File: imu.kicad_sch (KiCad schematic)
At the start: 2 parts, among them U1 BMI088

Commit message: Updated stm32
Updated stm32 and usb-c
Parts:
- renumbered C3 to C8
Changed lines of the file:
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@@
 	(wire
 		(pts
-			(xy 130.81 92.71) (xy 133.35 92.71)
+			(xy 129.54 92.71) (xy 133.35 92.71)
 		)
 		(stroke
@@
 		)
 	)
-	(hierarchical_label "IMU_SDA"
-		(shape passive)
-		(at 130.81 92.71 180)
-		(effects
-			(font
-				(size 1.27 1.27)
-			)
-			(justify right)
-		)
-	)
-	(hierarchical_label "IMU_SCL"
+	(global_label "INT_ACC"
+		(shape output)
+		(at 163.83 85.09 0)
+		(fields_autoplaced yes)
+		(effects
+			(font
+				(size 1.27 1.27)
+			)
+			(justify left)
+		)
+		(property "Intersheetrefs" "${INTERSHEET_REFS}"
+			(at 174.3143 85.09 0)
+			(hide yes)
+			(show_name no)
+			(do_not_autoplace no)
+			(effects
+				(font
+					(size 1.27 1.27)
+				)
+				(justify left)
+			)
+		)
+	)
+	(global_label "INT_GYR"
+		(shape output)
+		(at 163.83 90.17 0)
+		(fields_autoplaced yes)
+		(effects
+			(font
+				(size 1.27 1.27)
+			)
+			(justify left)
+		)
+		(property "Intersheetrefs" "${INTERSHEET_REFS}"
+			(at 174.3143 90.17 0)
+			(hide yes)
+			(show_name no)
+			(do_not_autoplace no)
+			(effects
+				(font
+					(size 1.27 1.27)
+				)
+				(justify left)
+			)
+		)
+	)
+	(global_label "IMU_SCL"
 		(shape input)
 		(at 130.81 90.17 180)
+		(fields_autoplaced yes)
 		(effects
 			(font
@@
 			(justify right)
 		)
-	)
-	(hierarchical_label "INT_GYR"
-		(shape output)
-		(at 163.83 90.17 0)
-		(effects
-			(font
-				(size 1.27 1.27)
-			)
-			(justify left)
-		)
-	)
-	(hierarchical_label "INT_ACC"
-		(shape output)
-		(at 163.83 85.09 0)
-		(effects
-			(font
-				(size 1.27 1.27)
-			)
-			(justify left)
+		(property "Intersheetrefs" "${INTERSHEET_REFS}"
+			(at 119.9629 90.17 0)
+			(hide yes)
+			(show_name no)
+			(do_not_autoplace no)
+			(effects
+				(font
+					(size 1.27 1.27)
+				)
+				(justify right)
+			)
+		)
+	)
+	(global_label "IMU_SDA"
+		(shape passive)
+		(at 129.54 92.71 180)
+		(fields_autoplaced yes)
+		(effects
+			(font
+				(size 1.27 1.27)
+			)
+			(justify right)
+		)
+		(property "Intersheetrefs" "${INTERSHEET_REFS}"
+			(at 119.7437 92.71 0)
+			(hide yes)
+			(show_name no)
+			(do_not_autoplace no)
+			(effects
+				(font
+					(size 1.27 1.27)
+				)
+				(justify right)
+			)
 		)
 	)
@@
 		(in_pos_files yes)
 		(dnp no)
-		(property "Reference" "C3"
+		(property "Reference" "C8"
 			(at 110.49 92.7099 0)
 			(show_name no)
@@
 			(project "Drone_FC_project"
 				(path "/3077c137-9a1a-496f-be15-3587b3336d21/ee62e42c-1ca0-4e46-9141-f640bba8485d"
-					(reference "C3")
+					(reference "C8")
 					(unit 1)
 				)

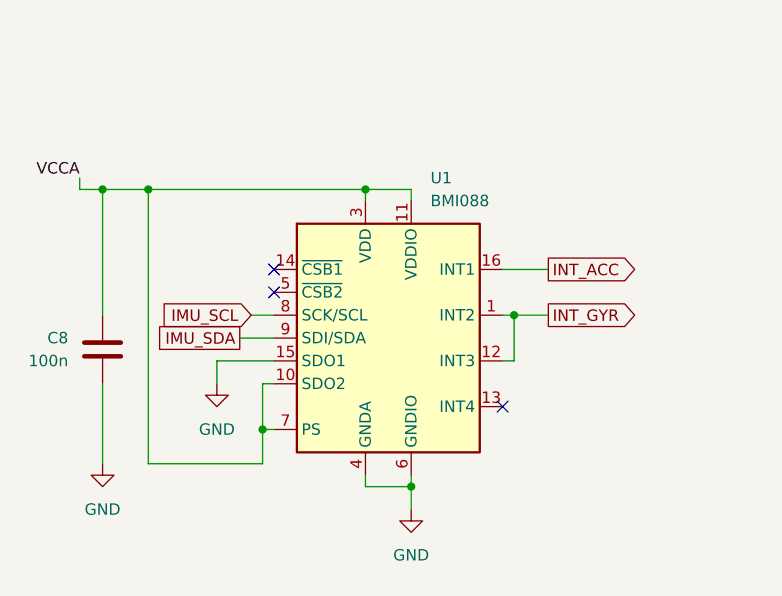
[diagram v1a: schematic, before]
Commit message: IMU, VBAT_Sense,
Fixed some decoupling issues, made the IMU into SPI mode. Wired all to stm32. Few updates on the appearances as well to make it look more organized.
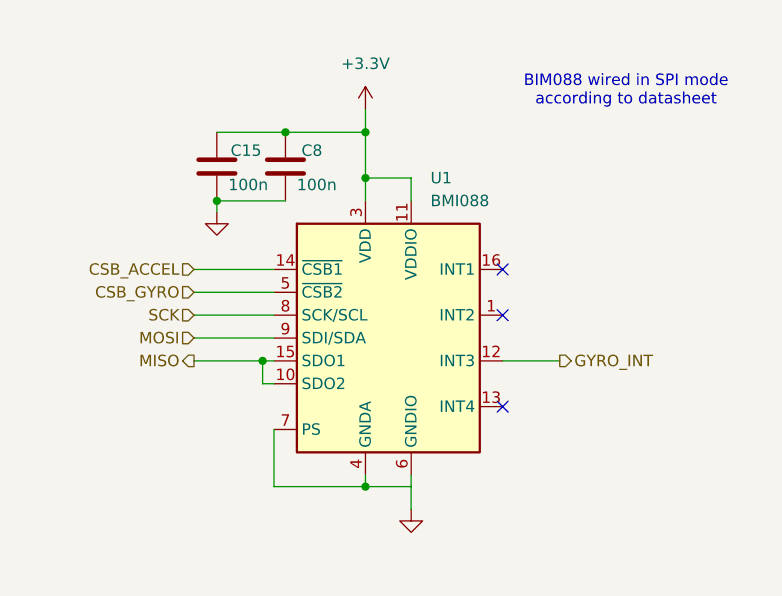
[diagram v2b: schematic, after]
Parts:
- added C15: 100n, Capacitor_SMD:C_0603_1608Metric, symbol Device:C
- C8: footprint Package_LGA:Bosch_LGA-16_4.5x3mm_P0.5mm_LayoutBorder7x1y_ClockwisePinNumbering -> Capacitor_SMD:C_0603_1608Metric
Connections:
- net GND: now also C15.2; no longer U1.15 (SDO1), U1.2 (GNDA), U1.4 (GNDA)
- net CSB_ACCEL: now reaches U1.14 (~{CSB1})
- net CSB_GYRO: now reaches U1.5 (~{CSB2})
- net IMU_SCL renamed SCK
- net IMU_SDA renamed MOSI
- net INT_ACC: no longer names the net of U1.16 (INT1)
- net INT_GYR: no longer names the net of U1.1 (INT2)
- net INT_GYR: no longer U1.12 (INT3)
- net VCCA renamed +3.3V
- net +3.3V: now also C15.1; no longer U1.10 (SDO2), U1.7 (PS)
- new net: U1.2 (GNDA), U1.4 (GNDA), U1.7 (PS)
- new net GYRO_INT: U1.12 (INT3)
- new net MISO: U1.10 (SDO2), U1.15 (SDO1)
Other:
- note added: "BIM088 wired in SPI mode according to datasheet"

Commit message: Created radio, cleanup a few other things
Finished radio schematic, added datasheets, added a stm32cubemx file for pinouts, added SPI1 and SPI2.
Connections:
- net MISO renamed SPI2_MISO
- net MOSI renamed SPI2_MOSI
- net SCK renamed SPI2_SCK
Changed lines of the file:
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@@
 		)
 	)
-	(hierarchical_label "MISO"
+	(hierarchical_label "SPI2_MISO"
 		(shape output)
 		(at 124.46 95.25 180)
@@
 		)
 	)
-	(hierarchical_label "SCK"
+	(hierarchical_label "SPI2_SCK"
 		(shape input)
 		(at 124.46 90.17 180)
@@
 		)
 	)
-	(hierarchical_label "MOSI"
+	(hierarchical_label "SPI2_MOSI"
 		(shape input)
 		(at 124.46 92.71 180)

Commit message: Fixing some radio things
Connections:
- net GND: now also U1.2 (GNDA), U1.4 (GNDA), U1.7 (PS)
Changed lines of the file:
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@@
 	(generator_version "10.0")
 	(paper "A4")
+	(rectangle
+		(start 109.22 57.15)
+		(end 181.61 119.38)
+		(stroke
+			(width 0)
+			(type default)
+		)
+		(fill
+			(type none)
+		)
+	)
 	(text "BIM088 wired in SPI mode\naccording to datasheet"
 		(exclude_from_sim no)
-		(at 172.466 65.278 0)
+		(at 165.1 66.04 0)
 		(effects
 			(font
@@
 	)
 	(junction
-		(at 143.51 109.22)
-		(diameter 0)
-		(color 0 0 0 0)
-	)
-	(junction
 		(at 143.51 74.93)
 		(diameter 0)
@@
 		(color 0 0 0 0)
 	)
+	(junction
+		(at 148.59 109.22)
+		(diameter 0)
+		(color 0 0 0 0)
+	)
 	(no_connect
 		(at 158.75 100.33)
@@
 	(wire
 		(pts
+			(xy 148.59 109.22) (xy 148.59 111.76)
+		)
+		(stroke
+			(width 0)
+			(type default)
+		)
+	)
+	(wire
+		(pts
 			(xy 124.46 85.09) (xy 133.35 85.09)
 		)
@@
 	(wire
 		(pts
+			(xy 132.08 102.87) (xy 133.35 102.87)
+		)
+		(stroke
+			(width 0)
+			(type default)
+		)
+	)
+	(wire
+		(pts
 			(xy 127 77.47) (xy 134.62 77.47)
 		)
@@
 	(wire
 		(pts
-			(xy 148.59 107.95) (xy 148.59 111.76)
+			(xy 148.59 107.95) (xy 148.59 109.22)
 		)
 		(stroke
@@
 	(wire
 		(pts
-			(xy 133.35 109.22) (xy 143.51 109.22)
-		)
-		(stroke
-			(width 0)
-			(type default)
-		)
-	)
-	(wire
-		(pts
-			(xy 143.51 109.22) (xy 148.59 109.22)
+			(xy 148.59 109.22) (xy 143.51 109.22)
 		)
 		(stroke
@@
 	(wire
 		(pts
-			(xy 133.35 102.87) (xy 133.35 109.22)
+			(xy 132.08 102.87) (xy 132.08 104.14)
 		)
 		(stroke
@@
 					(unit 1)
 				)
+			)
+		)
+	)
+	(symbol
+		(lib_id "power:GND")
+		(at 132.08 104.14 0)
+		(unit 1)
+		(body_style 1)
+		(exclude_from_sim no)
+		(in_bom yes)
+		(on_board yes)
+		(in_pos_files yes)
+		(dnp no)
+		(fields_autoplaced yes)
+		(property "Reference" "#PWR044"
+			(at 132.08 110.49 0)
+			(hide yes)
+			(show_name no)
+			(do_not_autoplace no)
+			(effects
+				(font
+					(size 1.27 1.27)
+				)
+			)
+		)
+		(property "Value" "GND"
+			(at 132.08 109.22 0)
+			(hide yes)
+			(show_name no)
+			(do_not_autoplace no)
+			(effects
+				(font
+					(size 1.27 1.27)
+				)
+			)
+		)
+		(property "Footprint" ""
+			(at 132.08 104.14 0)
+			(hide yes)
+			(show_name no)
+			(do_not_autoplace no)
+			(effects
+				(font
+					(size 1.27 1.27)
+				)
+			)
+		)
+		(property "Datasheet" ""
+			(at 132.08 104.14 0)
+			(hide yes)
+			(show_name no)
+			(do_not_autoplace no)
+			(effects
+				(font
+					(size 1.27 1.27)
+				)
+			)
+		)
+		(property "Description" "Power symbol creates a global label with name \"GND\" , ground"
+			(at 132.08 104.14 0)
+			(hide yes)
+			(show_name no)
+			(do_not_autoplace no)
+			(effects
+				(font
+					(size 1.27 1.27)
+				)
+			)
+		)
+		(pin "1"
+		)
+		(instances
+			(project "Drone_FC_project"
+				(path "/b2b6b395-2e98-42cf-8acc-86126f9affef/ee62e42c-1ca0-4e46-9141-f640bba8485d"
+					(reference "#PWR044")
+					(unit 1)
+				)

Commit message: footprints and spacing
Added half the footprints and made thigns look nicer.
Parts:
- C15, C8: footprint Capacitor_SMD:C_0603_1608Metric -> Capacitor_SMD:C_0402_1005Metric
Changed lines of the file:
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@@
 			)
 		)
-		(property "Footprint" "Capacitor_SMD:C_0603_1608Metric"
+		(property "Footprint" "Capacitor_SMD:C_0402_1005Metric"
 			(at 127.9652 77.47 0)
 			(hide yes)
@@
 			)
 		)
-		(property "Footprint" "Capacitor_SMD:C_0603_1608Metric"
+		(property "Footprint" "Capacitor_SMD:C_0402_1005Metric"
 			(at 135.5852 77.47 0)
 			(hide yes)

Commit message: more footprint work and downloaded some
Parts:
- U1: footprint Package_LGA:Bosch_LGA-16_4.5x3mm_P0.5mm_LayoutBorder7x1y_ClockwisePinNumbering -> drone_libary:LGA-16_Bosch_BMI088
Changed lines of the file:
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@@
 			)
 		)
-		(property "Footprint" "Package_LGA:Bosch_LGA-16_4.5x3mm_P0.5mm_LayoutBorder7x1y_ClockwisePinNumbering"
+		(property "Footprint" "drone_libary:LGA-16_Bosch_BMI088"
 			(at 129.54 93.98 0)
 			(hide yes)
